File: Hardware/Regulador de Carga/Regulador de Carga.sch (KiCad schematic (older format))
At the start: 20 parts, among them Q1 2N3904

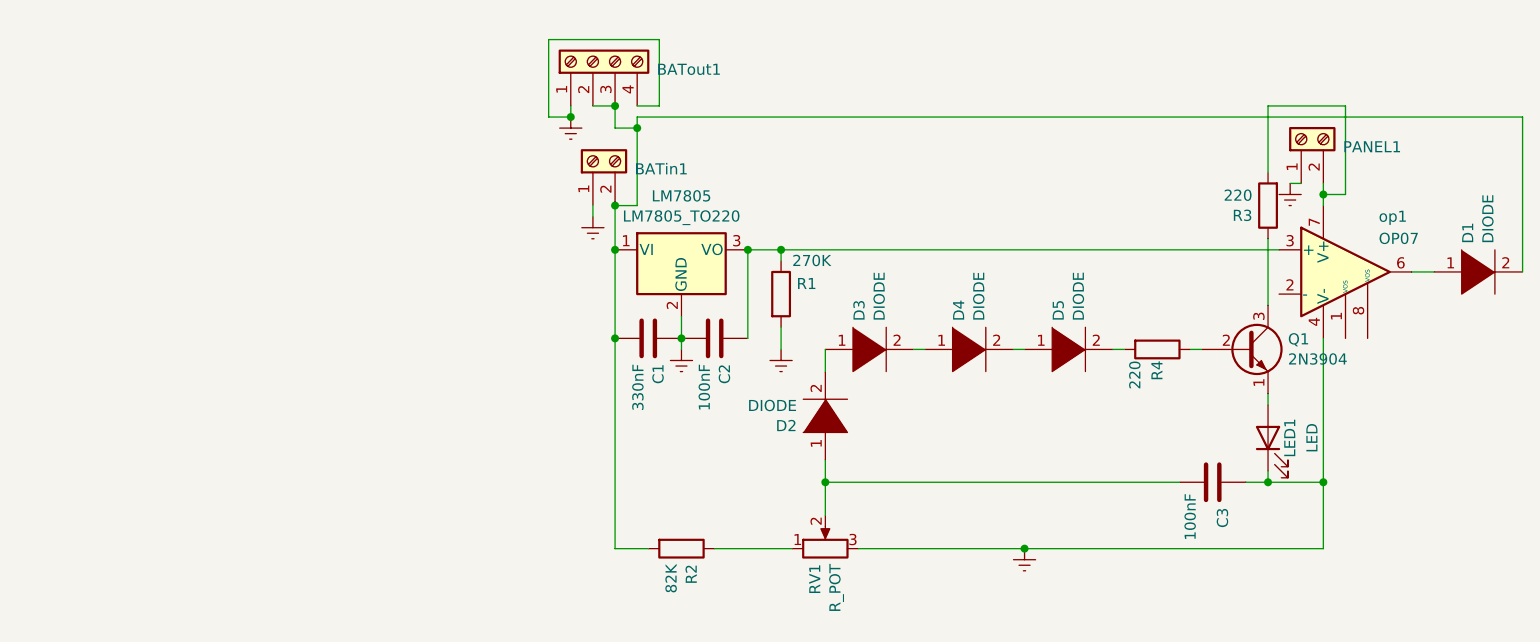
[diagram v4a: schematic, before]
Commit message: Actualizar el regulador de carga
Cambie los tres diodos y el transistor por un operacional en modo comparador.
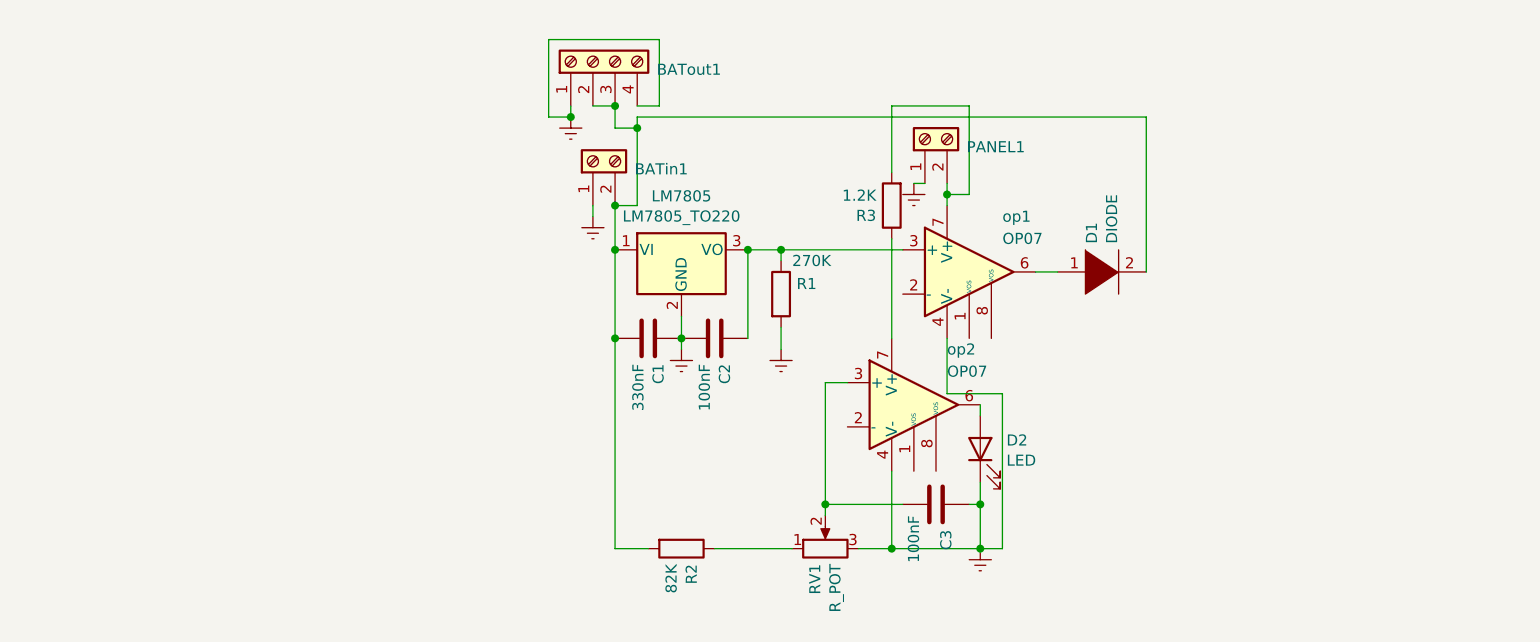
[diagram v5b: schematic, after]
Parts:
- removed D2, D3, D4, D5: DIODE, Diode_THT:D_A-405_P12.70mm_Horizontal, symbol pspice:DIODE
- removed LED1: LED, LED_THT:LED_D5.0mm, symbol Device:LED
- removed Q1: 2N3904, Package_TO_SOT_THT:TO-92_Inline, symbol Transistor_BJT:2N3904
- removed R4: 220, Resistor_THT:R_Axial_DIN0204_L3.6mm_D1.6mm_P7.62mm_Horizontal, symbol Device:R
- added D2: LED, LED_THT:LED_D3.0mm, symbol Device:LED
- added op2: OP07, Package_DIP:DIP-8_W7.62mm, symbol Amplifier_Operational:OP07
- R3: value 220 -> 1.2K
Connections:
- net Earth: now also D2.1 (K), op2.4 (V-)
- net at C3.2, RV1.2: now also op2.3 (+)
- net at R3.1: now also op2.7 (V+)
- new net: D2.2 (A), op2.6
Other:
- moved on the sheet: C3, D1, PANEL1, R3, op1
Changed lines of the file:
@@
 L Amplifier_Operational:OP07 op1
 U 1 1 5E9EA082
-P 7800 2850
-F 0 "op1" H 7950 3100 50  0000 L CNN
-F 1 "OP07" H 7950 3000 50  0000 L CNN
-F 2 "Package_DIP:DIP-8_W7.62mm" H 7850 2900 50  0001 C CNN
-F 3 "https://www.analog.com/media/en/technical-documentation/data-sheets/OP07.pdf" H 7850 3000 50  0001 C CNN
-	1    7800 2850
+P 6100 2850
+F 0 "op1" H 6250 3100 50  0000 L CNN
+F 1 "OP07" H 6250 3000 50  0000 L CNN
+F 2 "Package_DIP:DIP-8_W7.62mm" H 6150 2900 50  0001 C CNN
+F 3 "https://www.analog.com/media/en/technical-documentation/data-sheets/OP07.pdf" H 6150 3000 50  0001 C CNN
+	1    6100 2850
 	1    0    0    -1
 $EndComp
@@
 $EndComp
 $Comp
-L Device:LED LED1
-U 1 1 5E9EAEE0
-P 7450 3600
-F 0 "LED1" H 7450 3500 50  0000 C CNN
-F 1 "LED" H 7450 3400 50  0000 C CNN
-F 2 "LED_THT:LED_D5.0mm" H 7450 3600 50  0001 C CNN
-F 3 "~" H 7450 3600 50  0001 C CNN
-	1    7450 3600
-	0    -1   -1   0
-$EndComp
-$Comp
 L pspice:DIODE D1
 U 1 1 5E9E51EC
-P 8400 2850
-F 0 "D1" V 8354 2978 50  0000 L CNN
-F 1 "DIODE" V 8445 2978 50  0000 L CNN
-F 2 "Diode_THT:D_A-405_P12.70mm_Horizontal" H 8400 2850 50  0001 C CNN
-F 3 "~" H 8400 2850 50  0001 C CNN
-	1    8400 2850
+P 6700 2850
+F 0 "D1" V 6654 2978 50  0000 L CNN
+F 1 "DIODE" V 6745 2978 50  0000 L CNN
+F 2 "Diode_THT:D_A-405_P12.70mm_Horizontal" H 6700 2850 50  0001 C CNN
+F 3 "~" H 6700 2850 50  0001 C CNN
+	1    6700 2850
 	1    0    0    -1
 $EndComp
@@
 L Device:C C3
 U 1 1 5E9EDB4A
-P 7200 3800
-F 0 "C3" H 7315 3846 50  0000 L CNN
-F 1 "100nF" H 7250 3700 50  0000 L CNN
-F 2 "Capacitor_THT:C_Disc_D4.3mm_W1.9mm_P5.00mm" H 7238 3650 50  0001 C CNN
-F 3 "~" H 7200 3800 50  0001 C CNN
-	1    7200 3800
+P 5950 3900
+F 0 "C3" H 6065 3946 50  0000 L CNN
+F 1 "100nF" H 6000 3800 50  0000 L CNN
+F 2 "Capacitor_THT:C_Disc_D4.3mm_W1.9mm_P5.00mm" H 5988 3750 50  0001 C CNN
+F 3 "~" H 5950 3900 50  0001 C CNN
+	1    5950 3900
 	0    1    1    0
 $EndComp
@@
 L power:Earth #PWR0105
 U 1 1 5E9F166F
-P 6350 4100
-F 0 "#PWR0105" H 6350 3850 50  0001 C CNN
-F 1 "Earth" H 6350 3950 50  0001 C CNN
-F 2 "" H 6350 4100 50  0001 C CNN
-F 3 "~" H 6350 4100 50  0001 C CNN
-	1    6350 4100
+P 6150 4100
+F 0 "#PWR0105" H 6150 3850 50  0001 C CNN
+F 1 "Earth" H 6150 3950 50  0001 C CNN
+F 2 "" H 6150 4100 50  0001 C CNN
+F 3 "~" H 6150 4100 50  0001 C CNN
+	1    6150 4100
 	1    0    0    -1
 $EndComp
@@
 L Connector:Screw_Terminal_01x02 PANEL1
 U 1 1 5E9F9816
-P 7600 2250
-F 0 "PANEL1" V 7564 2062 50  0000 R CNN
-F 1 "Screw_Terminal_01x02" V 7550 3200 50  0001 R CNN
-F 2 "TerminalBlock:TerminalBlock_bornier-2_P5.08mm" H 7600 2250 50  0001 C CNN
-F 3 "~" H 7600 2250 50  0001 C CNN
-	1    7600 2250
+P 5900 2250
+F 0 "PANEL1" V 5864 2062 50  0000 R CNN
+F 1 "Screw_Terminal_01x02" V 5850 3200 50  0001 R CNN
+F 2 "TerminalBlock:TerminalBlock_bornier-2_P5.08mm" H 5900 2250 50  0001 C CNN
+F 3 "~" H 5900 2250 50  0001 C CNN
+	1    5900 2250
 	0    -1   -1   0
 $EndComp
@@
 L power:Earth #PWR0107
 U 1 1 5E9FBB4D
-P 7550 2450
-F 0 "#PWR0107" H 7550 2200 50  0001 C CNN
-F 1 "Earth" H 7550 2300 50  0001 C CNN
-F 2 "" H 7550 2450 50  0001 C CNN
-F 3 "~" H 7550 2450 50  0001 C CNN
-	1    7550 2450
-	1    0    0    -1
-$EndComp
-Wire Wire Line
-	7600 2450 7550 2450
+P 5850 2450
+F 0 "#PWR0107" H 5850 2200 50  0001 C CNN
+F 1 "Earth" H 5850 2300 50  0001 C CNN
+F 2 "" H 5850 2450 50  0001 C CNN
+F 3 "~" H 5850 2450 50  0001 C CNN
+	1    5850 2450
+	1    0    0    -1
+$EndComp
+Wire Wire Line
+	5900 2450 5850 2450
 Wire Wire Line
 	4500 2100 4500 2200
@@
 Connection ~ 4500 2550
 Wire Wire Line
-	8100 2850 8200 2850
-Wire Wire Line
-	8600 2850 8600 2150
+	6400 2850 6500 2850
+Wire Wire Line
+	6900 2850 6900 2150
 Wire Wire Line
 	4600 2150 4600 2200
 Connection ~ 4600 2200
 $Comp
-L Transistor_BJT:2N3904 Q1
-U 1 1 5EBEE765
-P 7350 3200
-F 0 "Q1" H 7540 3246 50  0000 L CNN
-F 1 "2N3904" H 7540 3155 50  0000 L CNN
-F 2 "Package_TO_SOT_THT:TO-92_Inline" H 7550 3125 50  0001 L CIN
-F 3 "https://www.fairchildsemi.com/datasheets/2N/2N3904.pdf" H 7350 3200 50  0001 L CNN
-	1    7350 3200
-	1    0    0    -1
-$EndComp
-$Comp
 L Device:R R3
 U 1 1 5EBF2660
-P 7450 2550
-F 0 "R3" H 7520 2596 50  0000 L CNN
-F 1 "220" H 7520 2505 50  0000 L CNN
-F 2 "Resistor_THT:R_Axial_DIN0204_L3.6mm_D1.6mm_P7.62mm_Horizontal" V 7380 2550 50  0001 C CNN
-F 3 "~" H 7450 2550 50  0001 C CNN
-	1    7450 2550
+P 5750 2550
+F 0 "R3" H 5820 2596 50  0000 L CNN
+F 1 "1.2K" H 5820 2505 50  0000 L CNN
+F 2 "Resistor_THT:R_Axial_DIN0204_L3.6mm_D1.6mm_P7.62mm_Horizontal" V 5680 2550 50  0001 C CNN
+F 3 "~" H 5750 2550 50  0001 C CNN
+	1    5750 2550
 	-1   0    0    1
 $EndComp
 Wire Wire Line
-	7700 2450 7700 2500
-Wire Wire Line
-	7700 2500 7800 2500
-Wire Wire Line
-	7800 2500 7800 2100
-Wire Wire Line
-	7800 2100 7450 2100
-Wire Wire Line
-	7450 2100 7450 2400
-Connection ~ 7700 2500
-Wire Wire Line
-	7700 2500 7700 2550
-Wire Wire Line
-	7450 2700 7450 3000
-Wire Wire Line
-	7450 3400 7450 3450
+	6000 2450 6000 2500
+Wire Wire Line
+	6000 2500 6100 2500
+Wire Wire Line
+	6100 2500 6100 2100
+Wire Wire Line
+	6100 2100 5750 2100
+Wire Wire Line
+	5750 2100 5750 2400
+Connection ~ 6000 2500
+Wire Wire Line
+	6000 2500 6000 2550
 Wire Wire Line
 	4500 4100 4650 4100
@@
 	4950 4100 5300 4100
 Wire Wire Line
-	5600 4100 6350 4100
-Wire Wire Line
-	5450 3800 5450 3950
-Wire Wire Line
-	7350 3800 7450 3800
-Wire Wire Line
-	7450 3800 7450 3750
-Wire Wire Line
-	7700 3150 7700 3800
-Wire Wire Line
-	7450 3800 7700 3800
-Connection ~ 7450 3800
-Connection ~ 7700 3800
-Wire Wire Line
-	7700 3800 7700 4100
-$Comp
-L Device:R R4
-U 1 1 5EBEB6D4
-P 6950 3200
-F 0 "R4" H 7000 3200 50  0000 L CNN
-F 1 "220" H 7000 3100 50  0000 L CNN
-F 2 "Resistor_THT:R_Axial_DIN0204_L3.6mm_D1.6mm_P7.62mm_Horizontal" V 6880 3200 50  0001 C CNN
-F 3 "~" H 6950 3200 50  0001 C CNN
-	1    6950 3200
-	0    1    1    0
-$EndComp
-$Comp
-L pspice:DIODE D5
-U 1 1 5ECF23A4
-P 6550 3200
-F 0 "D5" V 6504 3328 50  0000 L CNN
-F 1 "DIODE" V 6595 3328 50  0000 L CNN
-F 2 "Diode_THT:D_A-405_P12.70mm_Horizontal" H 6550 3200 50  0001 C CNN
-F 3 "~" H 6550 3200 50  0001 C CNN
-	1    6550 3200
-	1    0    0    -1
-$EndComp
-$Comp
-L pspice:DIODE D4
-U 1 1 5ECFBDFE
-P 6100 3200
-F 0 "D4" V 6054 3328 50  0000 L CNN
-F 1 "DIODE" V 6145 3328 50  0000 L CNN
-F 2 "Diode_THT:D_A-405_P12.70mm_Horizontal" H 6100 3200 50  0001 C CNN
-F 3 "~" H 6100 3200 50  0001 C CNN
-	1    6100 3200
-	1    0    0    -1
-$EndComp
-$Comp
-L pspice:DIODE D3
-U 1 1 5ECFC15C
-P 5650 3200
-F 0 "D3" V 5604 3328 50  0000 L CNN
-F 1 "DIODE" V 5695 3328 50  0000 L CNN
-F 2 "Diode_THT:D_A-405_P12.70mm_Horizontal" H 5650 3200 50  0001 C CNN
-F 3 "~" H 5650 3200 50  0001 C CNN
-	1    5650 3200
-	1    0    0    -1
-$EndComp
-$Comp
-L pspice:DIODE D2
-U 1 1 5ECFE728
-P 5450 3500
-F 0 "D2" V 5404 3628 50  0000 L CNN
-F 1 "DIODE" V 5495 3628 50  0000 L CNN
-F 2 "Diode_THT:D_A-405_P12.70mm_Horizontal" H 5450 3500 50  0001 C CNN
-F 3 "~" H 5450 3500 50  0001 C CNN
-	1    5450 3500
+	5600 4100 5750 4100
+$Comp
+L Amplifier_Operational:OP07 op2
+U 1 1 5EDD960A
+P 5850 3450
+F 0 "op2" H 6000 3700 50  0000 L CNN
+F 1 "OP07" H 6000 3600 50  0000 L CNN
+F 2 "Package_DIP:DIP-8_W7.62mm" H 5900 3500 50  0001 C CNN
+F 3 "https://www.analog.com/media/en/technical-documentation/data-sheets/OP07.pdf" H 5900 3600 50  0001 C CNN
+	1    5850 3450
+	1    0    0    -1
+$EndComp
+Wire Wire Line
+	5450 3350 5550 3350
+Wire Wire Line
+	5750 3750 5750 4100
+Wire Wire Line
+	5450 3350 5450 3900
+Wire Wire Line
+	5250 2750 5800 2750
+Connection ~ 5250 2750
+Wire Wire Line
+	5750 2700 5750 3150
+Wire Wire Line
+	6900 2150 4600 2150
+$Comp
+L Device:LED D2
+U 1 1 5EDE7369
+P 6150 3650
+F 0 "D2" V 6189 3532 50  0000 R CNN
+F 1 "LED" V 6098 3532 50  0000 R CNN
+F 2 "LED_THT:LED_D3.0mm" H 6150 3650 50  0001 C CNN
+F 3 "~" H 6150 3650 50  0001 C CNN
+	1    6150 3650
 	0    -1   -1   0
 $EndComp
 Wire Wire Line
-	5450 3800 7050 3800
-Wire Wire Line
-	5450 3800 5450 3700
-Connection ~ 5450 3800
-Wire Wire Line
-	5450 3300 5450 3200
-Wire Wire Line
-	5250 2750 7500 2750
-Connection ~ 5250 2750
-Wire Wire Line
-	4600 2150 8600 2150
-Wire Wire Line
-	7700 4100 6350 4100
-Connection ~ 6350 4100
-Wire Wire Line
-	5850 3200 5900 3200
-Wire Wire Line
-	6300 3200 6350 3200
-Wire Wire Line
-	6750 3200 6800 3200
-Wire Wire Line
-	7100 3200 7150 3200
+	6150 3450 6150 3500
+Wire Wire Line
+	6150 3800 6150 3900
+Wire Wire Line
+	6000 3150 6000 3400
+Wire Wire Line
+	6000 3400 6250 3400
+Wire Wire Line
+	6250 4100 6150 4100
+Connection ~ 6150 4100
+Wire Wire Line
+	5800 3900 5450 3900
+Connection ~ 5450 3900
+Wire Wire Line
+	5450 3900 5450 3950
+Wire Wire Line
+	5750 4100 6150 4100
+Connection ~ 5750 4100
+Wire Wire Line
+	6250 3400 6250 4100
+Wire Wire Line
+	6100 3900 6150 3900
+Connection ~ 6150 3900
+Wire Wire Line
+	6150 3900 6150 4100
 $EndSCHEMATC

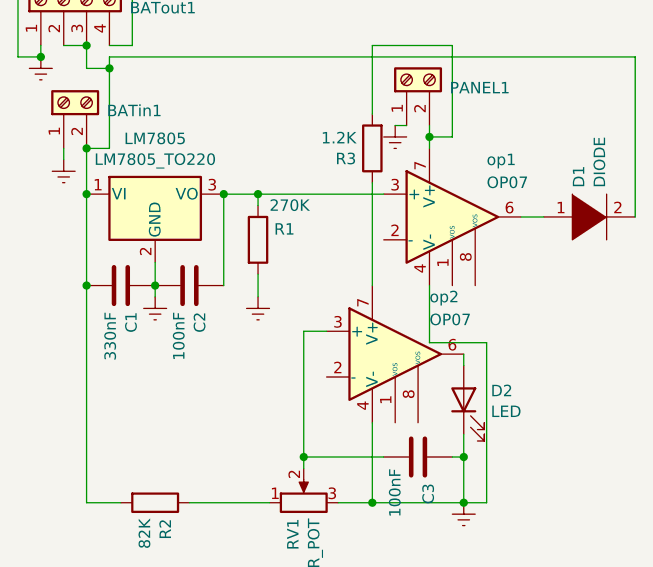
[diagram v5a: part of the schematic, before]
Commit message: Corregir errores del RC
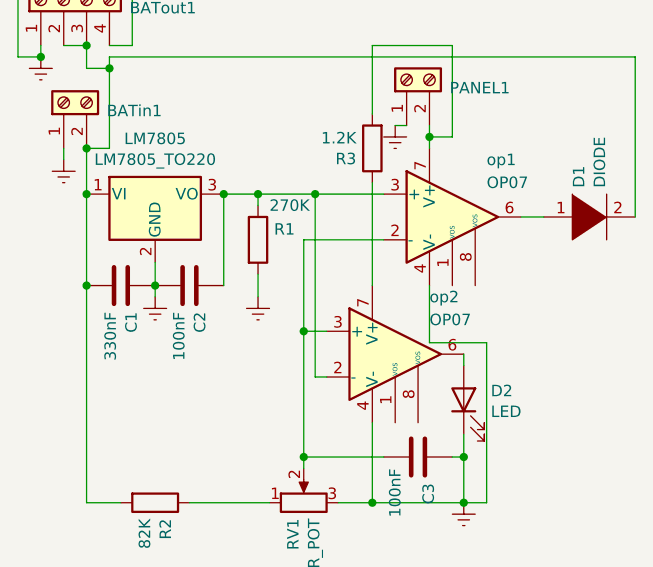
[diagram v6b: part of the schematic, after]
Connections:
- net at C2.1, LM7805.3 (VO), R1.1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: now also op2.2 (-)
- net at op1.2 (-): now also C3.2, RV1.2, op2.3 (+)
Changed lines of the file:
@@
 	5450 3350 5450 3900
 Wire Wire Line
-	5250 2750 5800 2750
+	5250 2750 5500 2750
 Connection ~ 5250 2750
 Wire Wire Line
@@
 Wire Wire Line
 	6150 3900 6150 4100
+Wire Wire Line
+	5550 3550 5500 3550
+Wire Wire Line
+	5500 3550 5500 2750
+Connection ~ 5500 2750
+Wire Wire Line
+	5500 2750 5800 2750
+Wire Wire Line
+	5800 2950 5450 2950
+Wire Wire Line
+	5450 2950 5450 3350
+Connection ~ 5450 3350
 $EndSCHEMATC

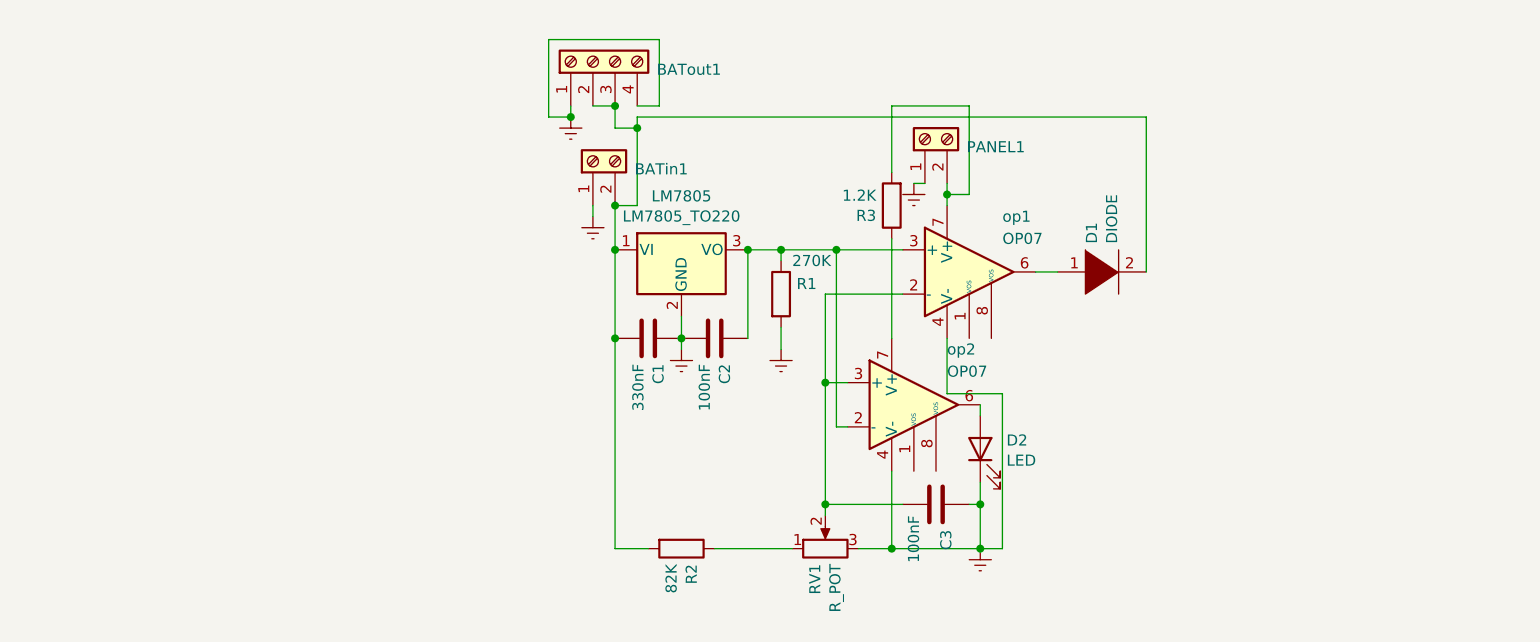
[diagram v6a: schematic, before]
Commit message: Actualizar el esquemático
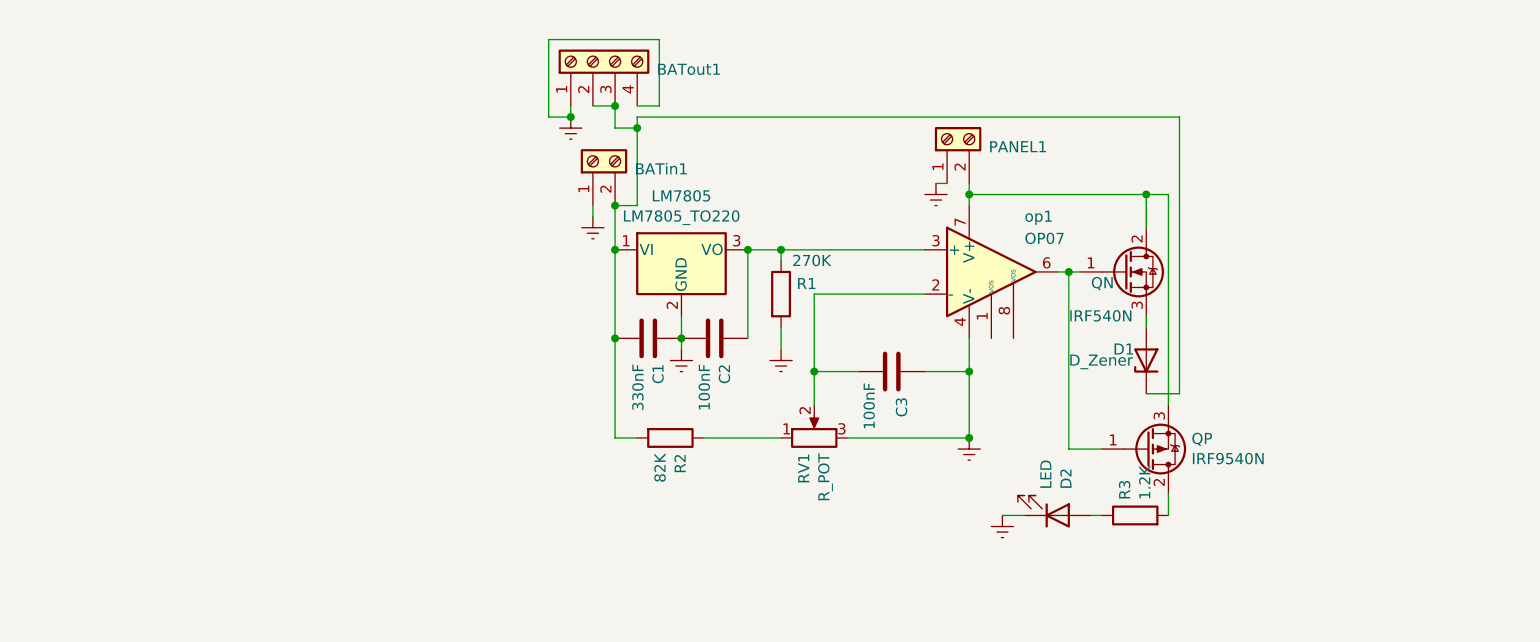
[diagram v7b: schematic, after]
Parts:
- removed D1: DIODE, Diode_THT:D_A-405_P12.70mm_Horizontal, symbol pspice:DIODE
- removed op2: OP07, Package_DIP:DIP-8_W7.62mm, symbol Amplifier_Operational:OP07
- added D1: D_Zener, Diode_THT:D_DO-15_P15.24mm_Horizontal, symbol Device:D_Zener
- added QN: IRF540N, Package_TO_SOT_THT:TO-220-3_Vertical, symbol Transistor_FET:IRF540N
- added QP: IRF9540N, Package_TO_SOT_THT:TO-220-3_Vertical, symbol Transistor_FET:IRF9540N
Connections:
- net at BATin1.2 (Pin_2), BATout1.2 (Pin_2), BATout1.3 (Pin_3)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: now also D1.1 (K)
- net at op1.6: now also QN.1 (G), QP.1 (G)
- net at PANEL1.2 (Pin_2), op1.7 (V+): now also QN.2 (D), QP.3 (S); no longer R3.2
- net at R3.1: now also D2.2 (A)
- new net: QP.2 (D), R3.2
- new net: D1.2 (A), QN.3 (S)
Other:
- moved on the sheet: C3, D2, PANEL1, R2, R3, RV1, op1

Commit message: Sacar captura para trello
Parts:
- D1: footprint Diode_THT:D_DO-15_P15.24mm_Horizontal -> Diode_THT:D_DO-15_P12.70mm_Horizontal
- renumbered QN to QN1, QP to QP1
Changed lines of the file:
@@
 Connection ~ 6100 3600
 $Comp
-L Transistor_FET:IRF9540N QP
+L Transistor_FET:IRF9540N QP1
 U 1 1 5EE20C18
 P 6900 3650
-F 0 "QP" H 7104 3604 50  0000 L CNN
-F 1 "IRF9540N" H 7104 3695 50  0000 L CNN
+F 0 "QP1" H 6700 3550 50  0000 L CNN
+F 1 "IRF9540N" H 6550 3500 50  0000 L CNN
 F 2 "Package_TO_SOT_THT:TO-220-3_Vertical" H 7100 3575 50  0001 L CIN
 F 3 "http://www.irf.com/product-info/datasheets/data/irf9540n.pdf" H 6900 3650 50  0001 L CNN
@@
 $EndComp
 $Comp
-L Transistor_FET:IRF540N QN
+L Transistor_FET:IRF540N QN1
 U 1 1 5EE22681
 P 6800 2850
-F 0 "QN" H 6650 2800 50  0000 L CNN
+F 0 "QN1" H 6650 2800 50  0000 L CNN
 F 1 "IRF540N" H 6550 2650 50  0000 L CNN
 F 2 "Package_TO_SOT_THT:TO-220-3_Vertical" H 7050 2775 50  0001 L CIN
@@
 F 0 "D1" V 6950 3400 50  0000 R CNN
 F 1 "D_Zener" V 6900 3600 50  0000 R CNN
-F 2 "Diode_THT:D_DO-15_P15.24mm_Horizontal" H 6900 3250 50  0001 C CNN
+F 2 "Diode_THT:D_DO-15_P12.70mm_Horizontal" H 6900 3250 50  0001 C CNN
 F 3 "~" H 6900 3250 50  0001 C CNN
 	1    6900 3250
@@
 	7050 2150 4600 2150
 $Comp
-L power:Earth #PWR?
+L power:Earth #PWR0106
 U 1 1 5EE2B989
 P 6250 3950
-F 0 "#PWR?" H 6250 3700 50  0001 C CNN
+F 0 "#PWR0106" H 6250 3700 50  0001 C CNN
 F 1 "Earth" H 6250 3800 50  0001 C CNN
 F 2 "" H 6250 3950 50  0001 C CNN
